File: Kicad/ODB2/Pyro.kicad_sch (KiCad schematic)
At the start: 30 parts, among them U11 TLV172IDCK, U12 74LVC2G08DP_125, U13 74AHC1G04, U14 TLV172IDCK

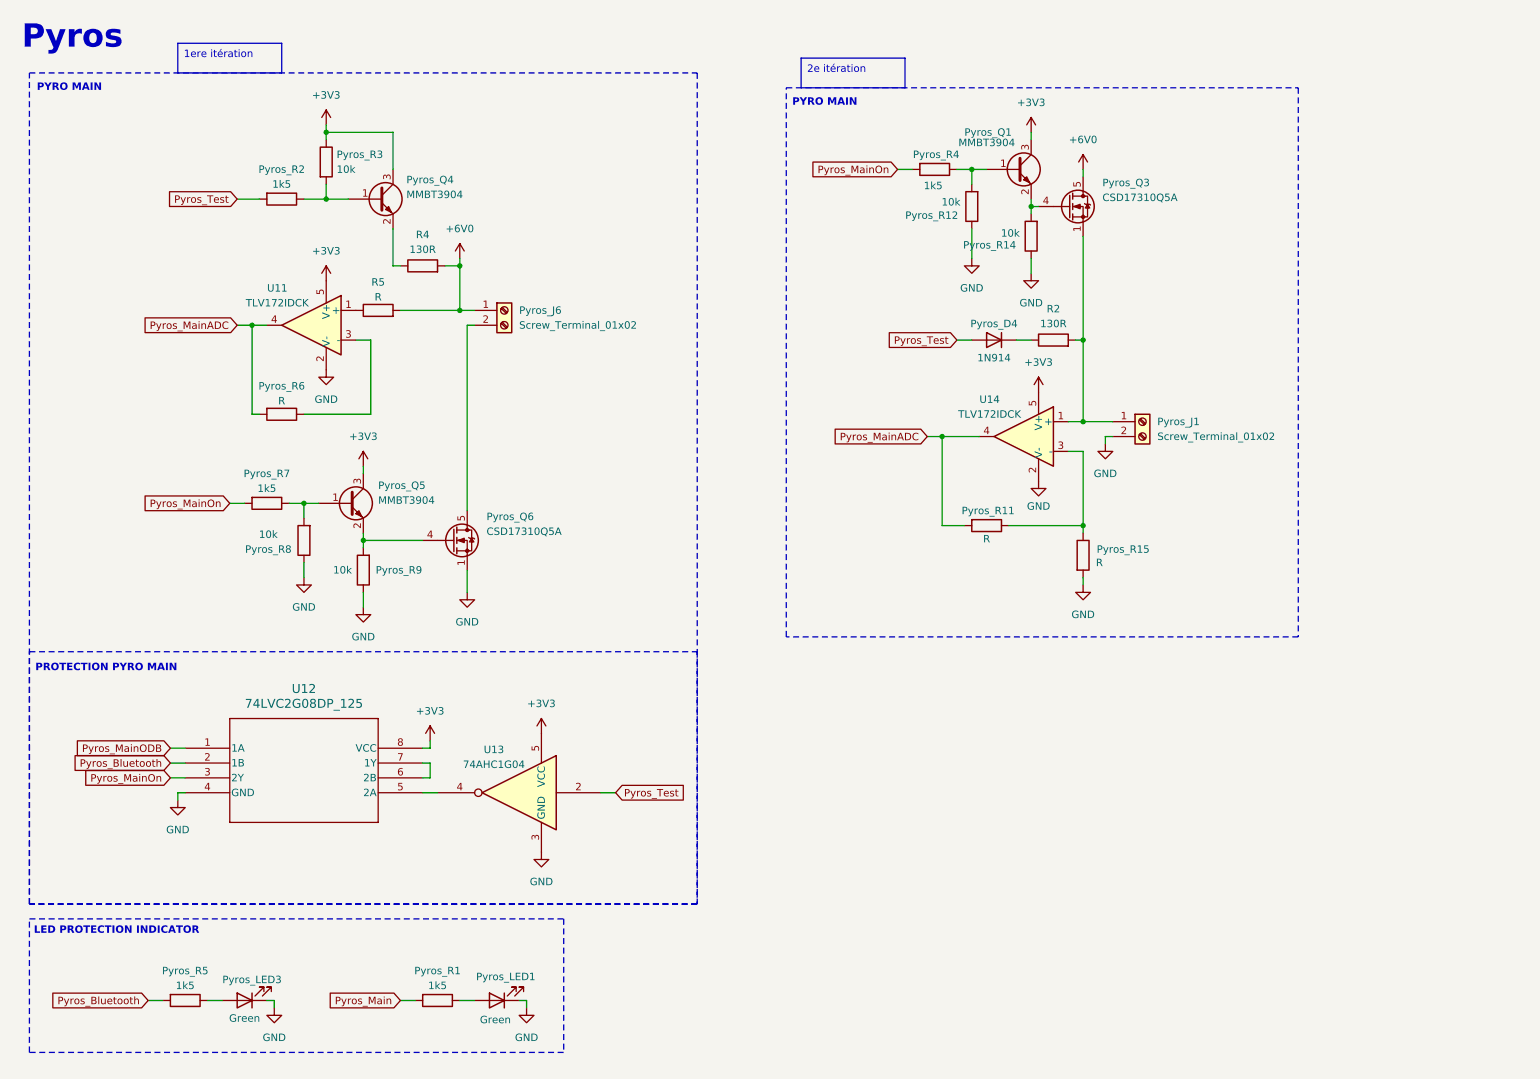
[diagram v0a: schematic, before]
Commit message: ajustement resistances et pyro_test 2e iteration
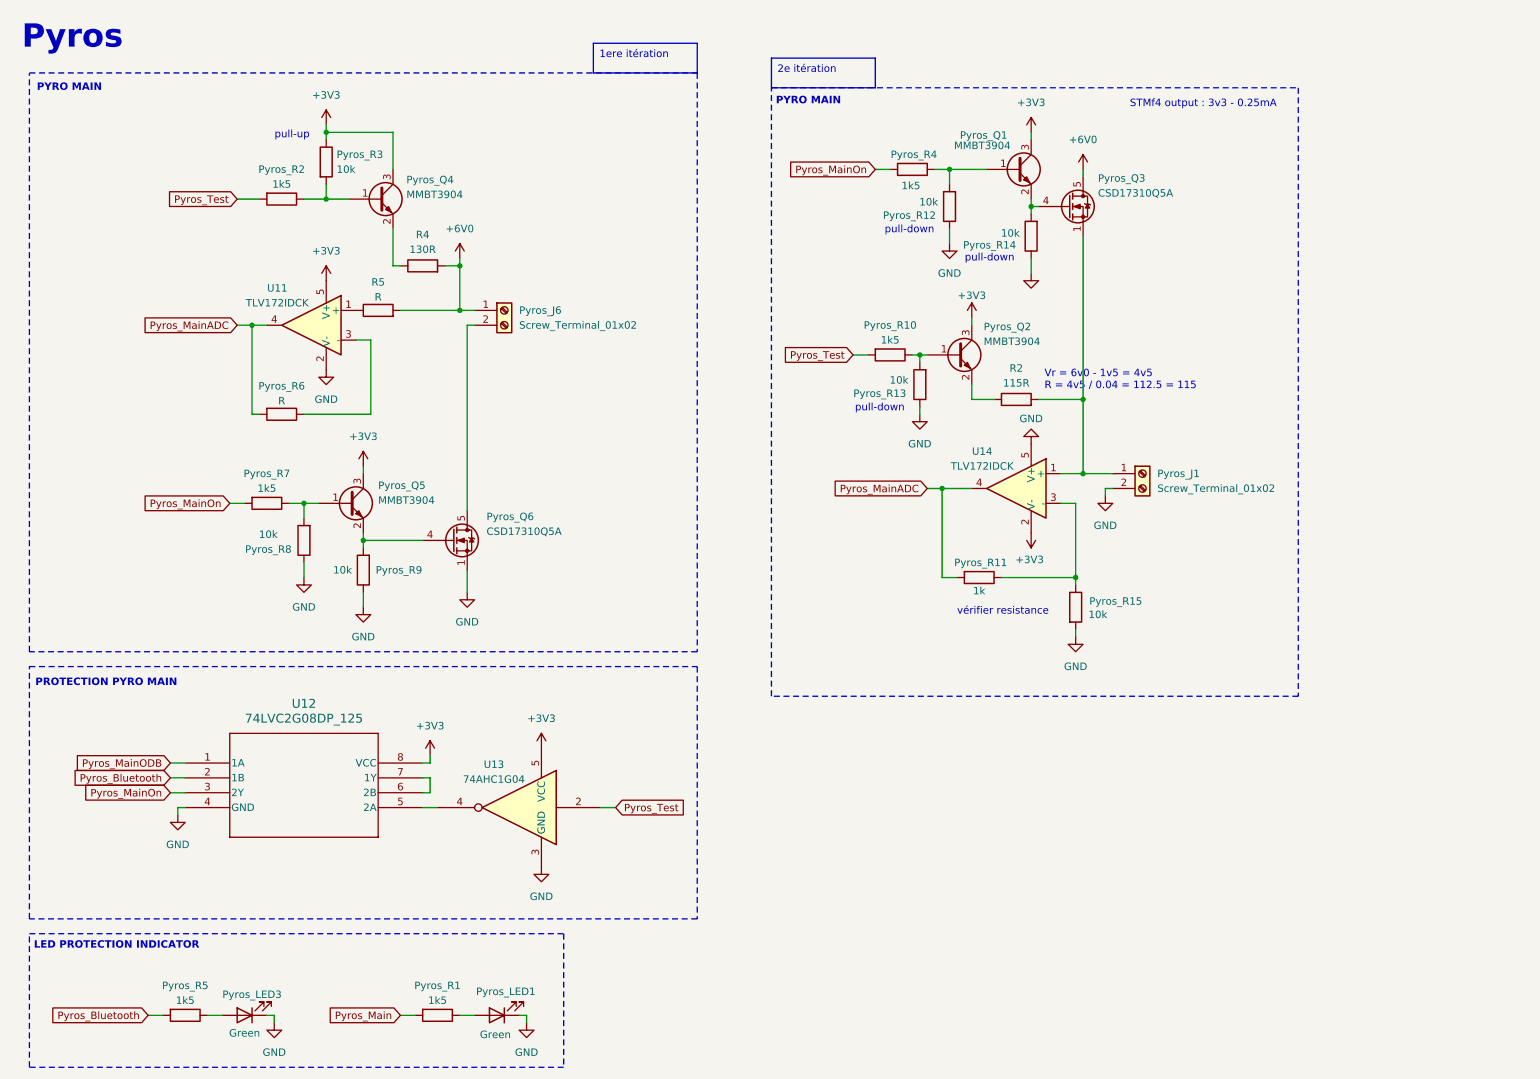
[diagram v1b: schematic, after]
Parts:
- removed Pyros_D4: 1N914, Diode_THT:D_DO-35_SOD27_P7.62mm_Horizontal, symbol Diode:1N914
- added Pyros_Q2: MMBT3904, Package_TO_SOT_SMD:SOT-23, symbol Transistor_BJT:MMBT3904
- added Pyros_R10: 1k5, symbol Device:R
- added Pyros_R13: 10k, symbol Device:R
- Pyros_R11: value R -> 1k
- Pyros_R15: value R -> 10k
- R2: value 130R -> 115R
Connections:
- net +3V3: now also U14.2 (V-), Pyros_Q2.3 (C); no longer U14.5 (V+)
- net GND: now also U14.5 (V+), Pyros_R13.1; no longer U14.2 (V-)
- net Pyros_Test: now also Pyros_R10.2
- net at R2.1: now also Pyros_Q2.2 (E)
- new net: Pyros_Q2.1 (B), Pyros_R10.1, Pyros_R13.2
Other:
- note added: "STMf4 output : 3v3 - 0.25mA"
- note added: "Vr = 6v0 - 1v5 = 4v5 R = 4v5 / 0.04 = 112.5 = 115"
- note added: "pull-down"
- note added: "pull-up"
- note added: "vérifier resistance"
- moved on the sheet: Pyros_J1, Pyros_LED1, Pyros_LED3, Pyros_R1, Pyros_R11, Pyros_R12, Pyros_R15, Pyros_R4, Pyros_R5, U12, U13, U14

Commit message: pyros
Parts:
- removed Pyros_Q1, Pyros_Q2, Pyros_Q4, Pyros_Q5: MMBT3904, Package_TO_SOT_SMD:SOT-23, symbol Transistor_BJT:MMBT3904
- removed Pyros_Q3: CSD17310Q5A, Package_TO_SOT_SMD:TDSON-8-1, symbol Transistor_FET:CSD17310Q5A
- removed Pyros_R15, Pyros_R3: 10k, symbol Device:R
- removed Pyros_R6, R5: R, symbol Device:R
- removed R2: 115R, symbol Device:R
- removed U11, U14: TLV172IDCK, Package_TO_SOT_SMD:SOT-353_SC-70-5, symbol Amplifier_Operational:TLV172IDCK
- removed U12: 74LVC2G08DP_125, TSSOP8_SOT505-2_NEX, symbol ODB_Lib:74LVC2G08DP_125
- removed U13: 74AHC1G04, symbol 74xGxx:74AHC1G04
- added Pyros_LED2: Green, symbol Device:LED
- added Pyros_MOSFET2: CSD17310Q5A, Package_TO_SOT_SMD:TDSON-8-1, symbol Transistor_FET:CSD17310Q5A
- added Pyros_NPN1, Pyros_NPN2: MMBT3904, Package_TO_SOT_SMD:SOT-23, symbol Transistor_BJT:MMBT3904
- added Pyros_R1, Pyros_R17, Pyros_R8: 1k5, symbol Device:R
- added Pyros_R5: 10k, symbol Device:R
- added U11: TLV2372, symbol Amplifier_Operational:TLV2372
- added U12: 74HC08D_653, SO14_SOT108-1_NEX, symbol ODB_Lib:74HC08D_653
- Pyros_R10: value 1k5 -> 68R ±1%
- Pyros_R11: value 1k -> 390R ±1%
- Pyros_R13: value 10k -> 1k5
- Pyros_R2: value 1k5 -> 10k
- Pyros_R3: renamed from R4; value 130R -> 68R ±1%
- Pyros_R4: value 1k5 -> 390R ±1%
- renumbered Pyros_Q6 to Pyros_MOSFET1, Pyros_R5 to Pyros_R15, Pyros_R1 to Pyros_R16, Pyros_R7 to Pyros_R6, Pyros_R8 to Pyros_R7
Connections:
- net Pyros_Main is gone; now on net Pyros_MainOn: Pyros_R16.2
- net +3V3: now also Pyros_NPN1.3 (C), Pyros_NPN2.3 (C), U11.8 (V+), U12.14 (VCC)
- net +6V0: now also Pyros_J1.1 (Pin_1), Pyros_R10.2, U11.3 (+), U11.5 (+)
- net GND: now also Pyros_R12.2, Pyros_R2.1, Pyros_LED2.1 (K), Pyros_MOSFET2.1 (S), Pyros_MOSFET2.2 (S), Pyros_MOSFET2.3 (S), Pyros_R5.2, U11.4 (V-), U12.7 (GND); no longer Pyros_J1.2 (Pin_2), Pyros_R12.1, Pyros_R13.1
- net Pyros_Bluetooth: now also U12.12 (4A), U12.2 (1B)
- net Pyros_MainADC: now also Pyros_R4.2, U11.1; no longer Pyros_R11.2
- net Pyros_MainODB: now also U12.1 (1A)
- net Pyros_MainOn: now also U12.6 (2Y); no longer Pyros_R4.2
- net Pyros_Test: now also Pyros_R1.2, Pyros_R8.2; no longer Pyros_R10.2, Pyros_R2.2
- net at Pyros_R4.1: now also Pyros_R5.1, U11.2 (-); no longer Pyros_R12.2
- net at Pyros_R10.1: now also Pyros_NPN2.2 (E); no longer Pyros_R13.2
- net at Pyros_R6.1, Pyros_R7.2: now also Pyros_MOSFET1.4 (G)
- net at Pyros_R9.2: now also Pyros_NPN2.1 (B), Pyros_R8.1; no longer Pyros_MOSFET1.4 (G)
- net at Pyros_R14.2: now also Pyros_R13.1, Pyros_MOSFET2.4 (G)
- net at Pyros_R11.1: now also Pyros_R12.1, U11.6 (-)
- net at Pyros_R3.1: now also Pyros_NPN1.2 (E)
- new net: Pyros_J1.2 (Pin_2), Pyros_MOSFET2.5 (D)
- new net: U12.10 (3B), U12.11 (4Y)
- new net: U12.3 (1Y), U12.4 (2A)
- new net: Pyros_NPN1.1 (B), Pyros_R1.1, Pyros_R2.2
- new net: Pyros_LED2.2 (A), Pyros_R17.1
- new net 6vEnable: U12.5 (2B), U12.9 (3A)
- new net Pyros_DrogueADC: Pyros_R11.2, U11.7
- new net Pyros_DrogueODB: U12.13 (4B)
- new net Pyros_DrogueOn: Pyros_R13.2, Pyros_R17.2, U12.8 (3Y)
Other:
- note added: "Enable 6v0 software -> 6v0 isolation"
- note added: "On = ODB x Bluetooth x 6vEnable"
- note added: "PROTECTION PYROS"
- note added: "PYRO DROGUE"
- note removed: "PROTECTION PYRO MAIN"
- note removed: "STMf4 output : 3v3 - 0.25mA"
- note removed: "Vr = 6v0 - 1v5 = 4v5 R = 4v5 / 0.04 = 112.5 = 115"
- note removed: "pull-up"
- note removed: "vérifier resistance"
- moved on the sheet: Pyros_J6, Pyros_MOSFET1, Pyros_R3, Pyros_R6, Pyros_R7

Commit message: fix and gate
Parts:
- removed Pyros_J1: Screw_Terminal_01x02, symbol Connector:Screw_Terminal_01x02
- removed Pyros_MOSFET2: CSD17310Q5A, Package_TO_SOT_SMD:TDSON-8-1, symbol Transistor_FET:CSD17310Q5A
- removed Pyros_R10: 68R ±1%, symbol Device:R
- removed Pyros_R11: 390R ±1%, symbol Device:R
- removed Pyros_R12, Pyros_R14, Pyros_R9: 10k, symbol Device:R
- removed Pyros_R13: 1k5, symbol Device:R
- removed unit 2 of U11
- removed U12: 74HC08D_653, SO14_SOT108-1_NEX, symbol ODB_Lib:74HC08D_653
- added U12: 74LVC2G08GT_115, Library:XSON8_SOT833-1_NEX, symbol ODB_Lib:74LVC2G08GT_115
- Pyros_R8: value 1k5 -> 10k
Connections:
- net +3V3: now also U12.8 (VCC)
- net GND: now also Pyros_R8.1, U12.4 (GND)
- net Pyros_Bluetooth: now also U12.2 (1B), U12.5 (2A)
- net Pyros_DrogueODB: now also U12.6 (2B)
- net Pyros_DrogueOn: now also U12.3 (2Y)
- net Pyros_MainODB: now also U12.1 (1A)
- net Pyros_MainOn: now also U12.7 (1Y)
- net Pyros_Test: no longer Pyros_R8.2
- net at Pyros_R6.1, Pyros_R7.2: now also Pyros_NPN2.1 (B); no longer Pyros_MOSFET1.4 (G)
- net at Pyros_NPN2.2 (E): now also Pyros_MOSFET1.4 (G), Pyros_R8.2
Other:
- note added: "Fire = On x 6V0"
- note added: "On = ODB x Bluetooth"
- note removed: "On = ODB x Bluetooth x 6vEnable"
- note removed: "PYRO DROGUE"
- moved on the sheet: Pyros_J6, Pyros_LED1, Pyros_LED2, Pyros_LED3, Pyros_MOSFET1, Pyros_NPN1, Pyros_R1, Pyros_R15, Pyros_R16, Pyros_R17, Pyros_R2, Pyros_R3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

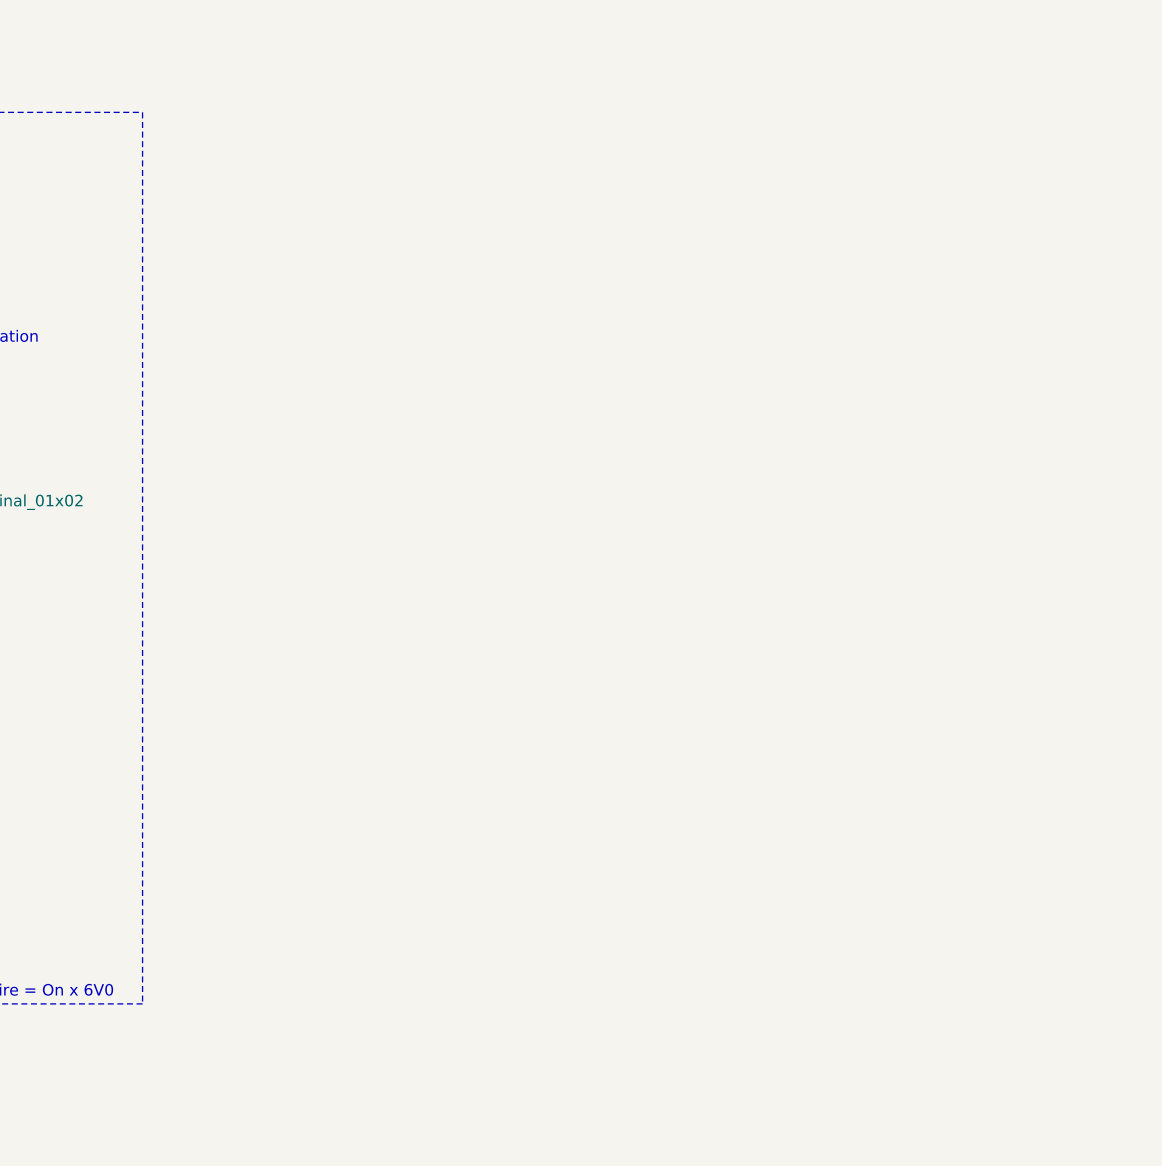
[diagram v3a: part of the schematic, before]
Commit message: add pyro drogue
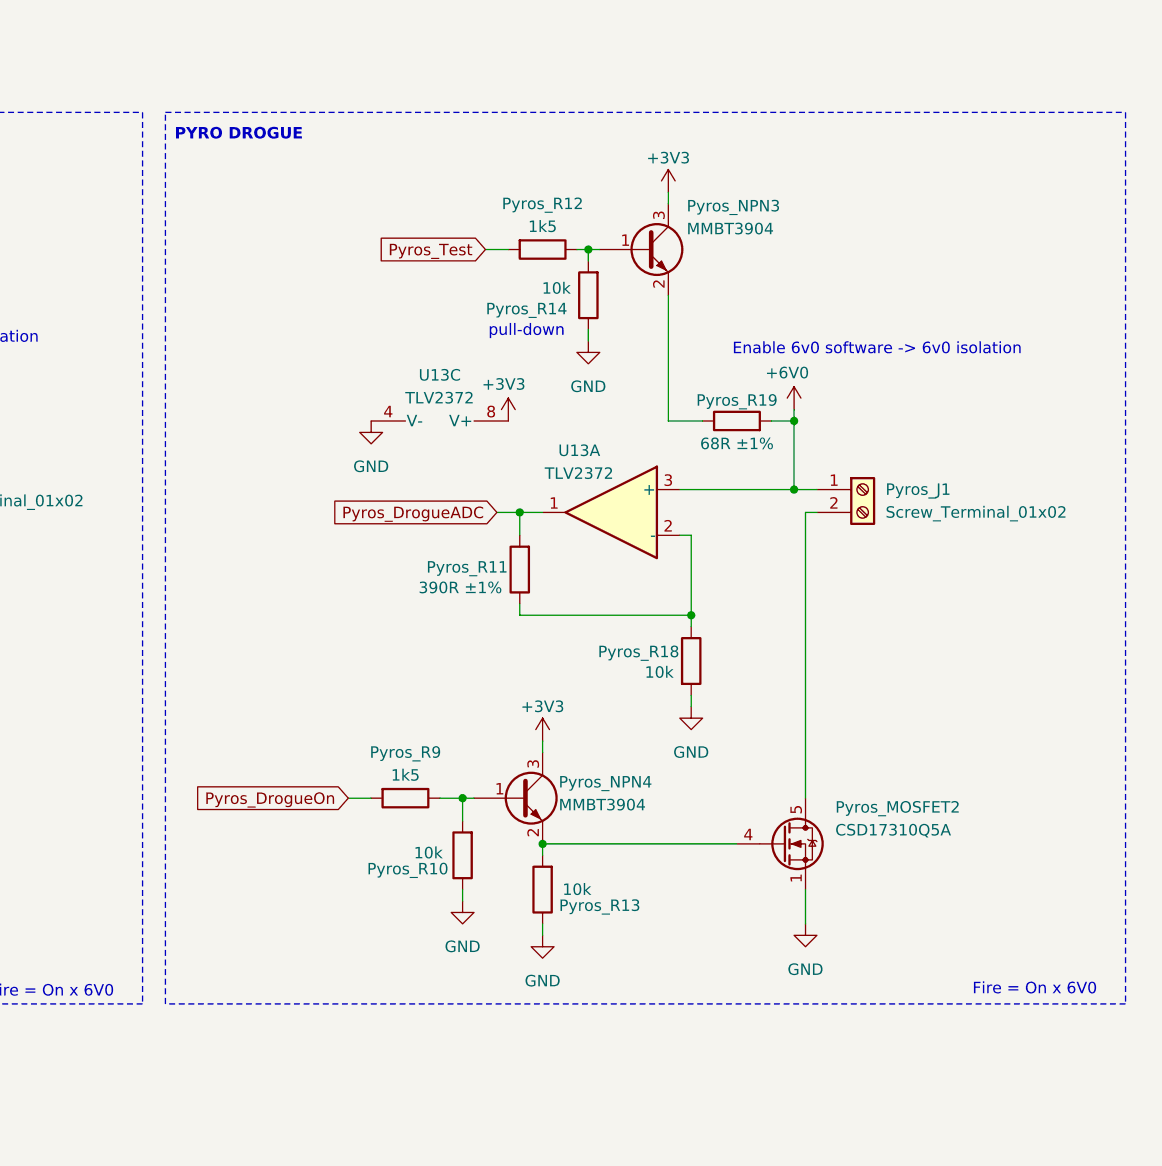
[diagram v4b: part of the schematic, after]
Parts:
- added Pyros_J1: Screw_Terminal_01x02, symbol Connector:Screw_Terminal_01x02
- added Pyros_MOSFET2: CSD17310Q5A, Package_TO_SOT_SMD:TDSON-8-1, symbol Transistor_FET:CSD17310Q5A
- added Pyros_NPN3, Pyros_NPN4: MMBT3904, Package_TO_SOT_SMD:SOT-23, symbol Transistor_BJT:MMBT3904
- added Pyros_R10, Pyros_R13, Pyros_R14, Pyros_R18: 10k, symbol Device:R
- added Pyros_R11: 390R ±1%, symbol Device:R
- added Pyros_R12, Pyros_R9: 1k5, symbol Device:R
- added Pyros_R19: 68R ±1%, symbol Device:R
- added U13: TLV2372, symbol Amplifier_Operational:TLV2372
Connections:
- net +3V3: now also Pyros_NPN3.3 (C), Pyros_NPN4.3 (C), U13.8 (V+)
- net +6V0: now also Pyros_J1.1 (Pin_1), Pyros_R19.2, U13.3 (+)
- net GND: now also Pyros_MOSFET2.1 (S), Pyros_MOSFET2.2 (S), Pyros_MOSFET2.3 (S), Pyros_R10.1, Pyros_R13.1, Pyros_R14.1, Pyros_R18.2, U13.4 (V-)
- net Pyros_DrogueOn: now also Pyros_R9.2
- net Pyros_Test: now also Pyros_R12.2
- new net: Pyros_NPN3.1 (B), Pyros_R12.1, Pyros_R14.2
- new net: Pyros_R11.1, Pyros_R18.1, U13.2 (-)
- new net: Pyros_NPN4.1 (B), Pyros_R10.2, Pyros_R9.1
- new net: Pyros_J1.2 (Pin_2), Pyros_MOSFET2.5 (D)
- new net: Pyros_MOSFET2.4 (G), Pyros_NPN4.2 (E), Pyros_R13.2
- new net: Pyros_NPN3.2 (E), Pyros_R19.1
- new net Pyros_DrogueADC: Pyros_R11.2, U13.1
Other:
- note added: "PYRO DROGUE"
